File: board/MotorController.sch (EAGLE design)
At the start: 35 parts, among them IC1 ATMEGA328P-PU, Q1 IPP80P03P4L-04, Q2 16Mhz, T1 BT137-600E

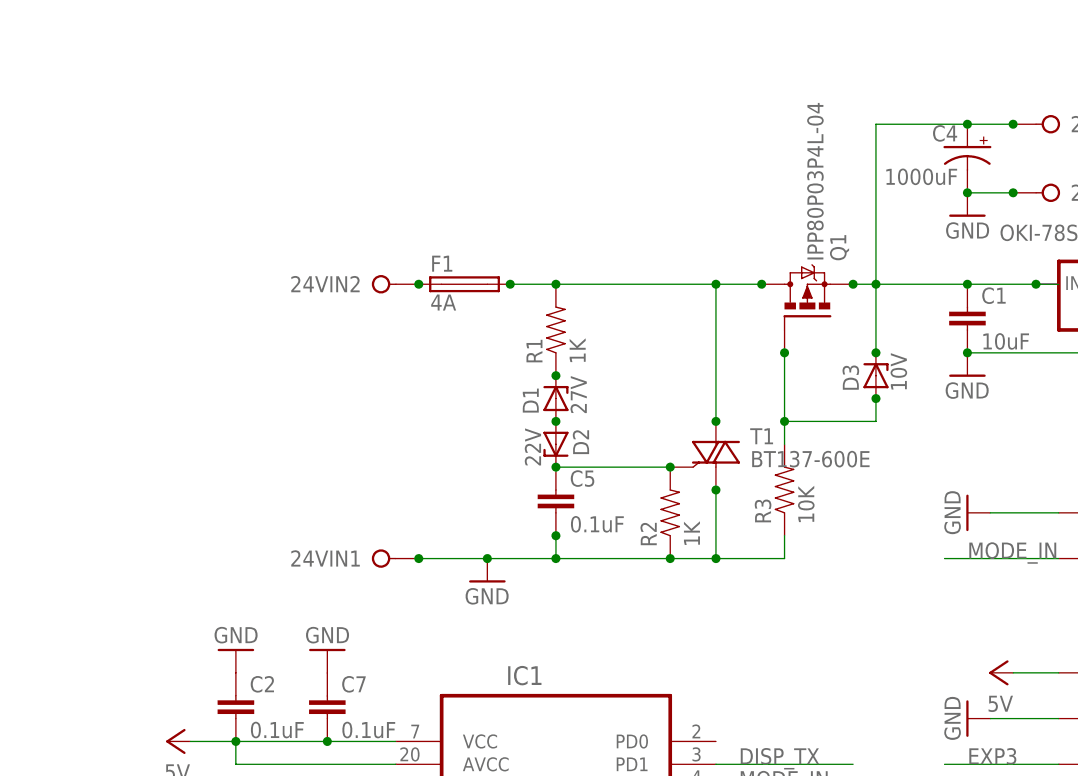
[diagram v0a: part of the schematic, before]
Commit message: Add soft-start capability to avoid high inrush current
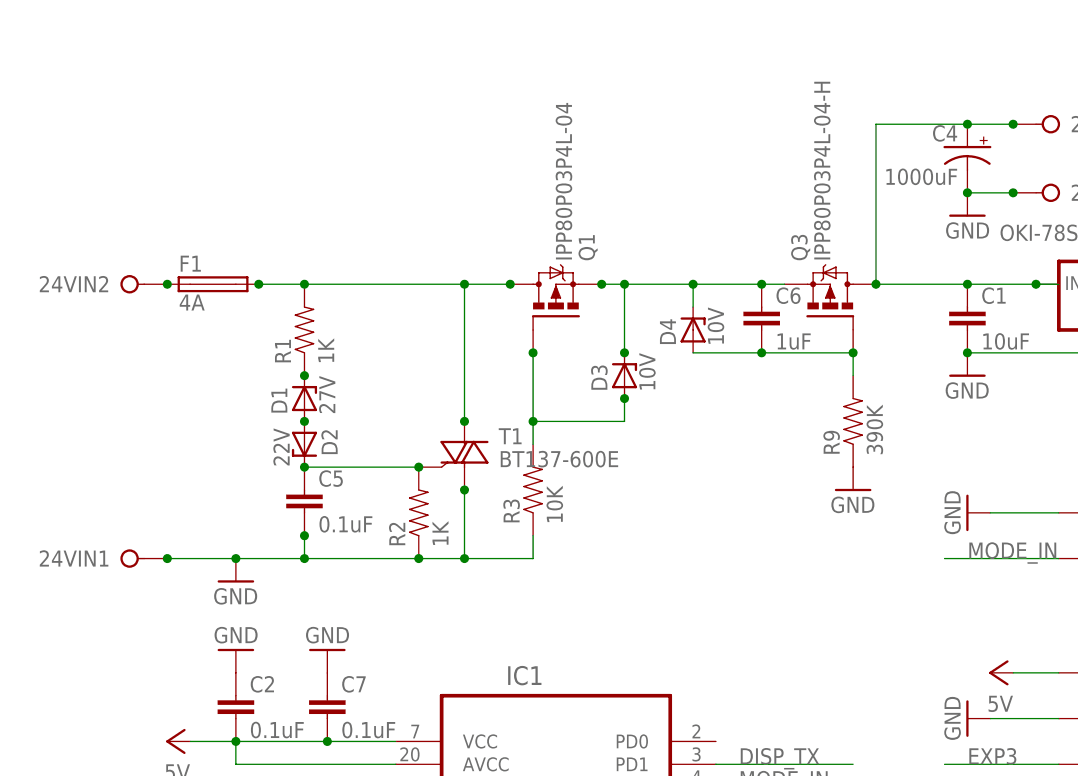
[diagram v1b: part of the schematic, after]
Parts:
- added C6: 1uF, SaintGimp:CAPACITOR-2.5MM
- added D4: 10V, SaintGimp:ZENER-7.5
- added Q3: IPP80P03P4L-04-H, SaintGimp:IPP80P03P4L-04-H
- added R9: 390K, SaintGimp:RESISTOR-7.5MM
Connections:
- new net N$11: C6.2, D4.A, Q3.G, R9.2
- new net N$9: C6.1, D3.C, D4.C, Q1.S, Q3.S
- net 24V-PROTECTED: now also Q3.D; no longer D3.C, Q1.S
- net GND: now also R9.1
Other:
- moved on the sheet: 24VIN1, 24VIN2, C5, D1, D2, D3, F1, Q1, R1, R2, R3, T1

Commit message: Many changes for version 3
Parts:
- removed C12: 20pF, SaintGimp:CAPACITOR-2.5MM
- removed Q3: IPP80P03P4L-04-H, SaintGimp:IPP80P03P4L-04-H
- added C10: 1uF, SaintGimp:CAPACITOR-2.5MM
- added Y1: 16Mhz, SaintGimp:CRYSTAL-V
- C1: value 10uF -> 0.1uF; device SaintGimp:CAPACITOR-5MM -> SaintGimp:CAPACITOR-2.5MM
- C11: value 20pF -> 1000uF; device SaintGimp:CAPACITOR-2.5MM -> SaintGimp:CAP-POL-25-14
- C3: value 10uF -> 20pF; device SaintGimp:CAPACITOR-5MM -> SaintGimp:CAPACITOR-2.5MM
- C4: value 1000uF -> 1uF; device SaintGimp:CAP-POL-25-14 -> SaintGimp:CAPACITOR-2.5MM
- C5: value 0.1uF -> 1uF
- C6: value 1uF -> 20pF
- C8, C9: value 1uF -> 10uF; device SaintGimp:CAPACITOR-2.5MM -> SaintGimp:CAPACITOR-5MM
- D1: value 27V -> 22V
- D2: value 22V -> 27V
- Q2: value 16Mhz -> SUP75P03-07-H; device SaintGimp:CRYSTAL-V -> SaintGimp:SUP75P03-07-H
- R1: value 1K -> 68
- R2: value 1K -> 10K
- R3: value 10K -> 220
- R5: value 220 -> 1K
- R6: value 68 -> 1K
- R7: value 390K -> 576K
- renumbered R9 to R7
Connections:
- net 24V: now also R6.2; no longer R1.2
- net 24V-PROTECTED: now also C11.+, C8.1, Q2.D; no longer C1.1, C4.+, Q3.D
- net CRYSTAL1: now also C3.1, Y1.2; no longer C11.1, Q2.2
- net CRYSTAL2: now also C6.1, Y1.1; no longer C12.1, Q2.1
- net DISP_TX: now also R1.2; no longer R6.2
- net GND: now also C1.1, C11.-, C4.2, C6.2, C7.2, R5.1, R8.1; no longer C1.2, C11.2, C12.2, C4.-, C7.1, R2.1, R3.1
- net N$1: now also C4.1, R3.1; no longer C8.1, R5.1
- net N$10: now also C5.1, R4.2; no longer C9.1, R5.2
- net N$11: now also C10.2, Q2.G; no longer C6.2, Q3.G
- net N$4: now also R8.2; no longer R3.2
- net N$5: now also D2.C, R6.1; no longer D1.C, R1.1
- net N$7: now also C7.1, D1.C, R5.2; no longer C5.1, D2.C, R2.2
- net N$8: now also R1.1; no longer R6.1
- net N$9: now also C10.1, Q2.S; no longer C6.1, Q3.S
- net RESET: now also R2.2; no longer R8.2
- net SPD_OUT: now also R3.2; no longer R4.2
- net VCC: now also C1.2, C9.1, R2.1; no longer C3.1, C7.2, R8.1
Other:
- moved on the sheet: C1, C3, C5, C6, C7, C8, C9, D1, D2, R1, R2, R3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

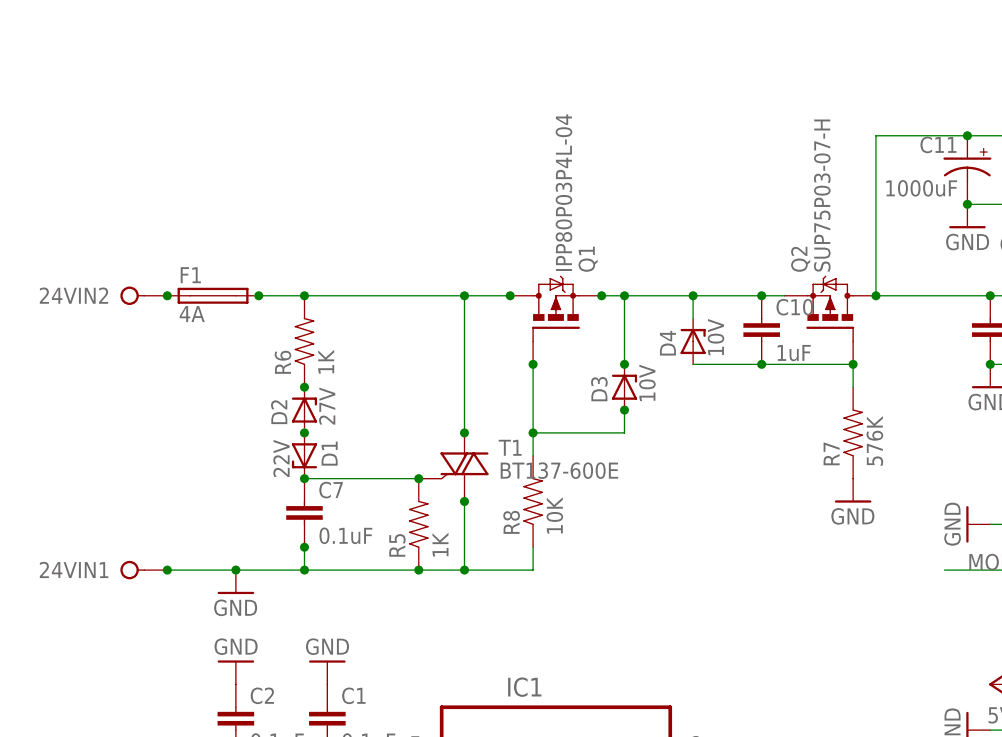
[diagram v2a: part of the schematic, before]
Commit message: Tweak TO220 packages and add board heatsink
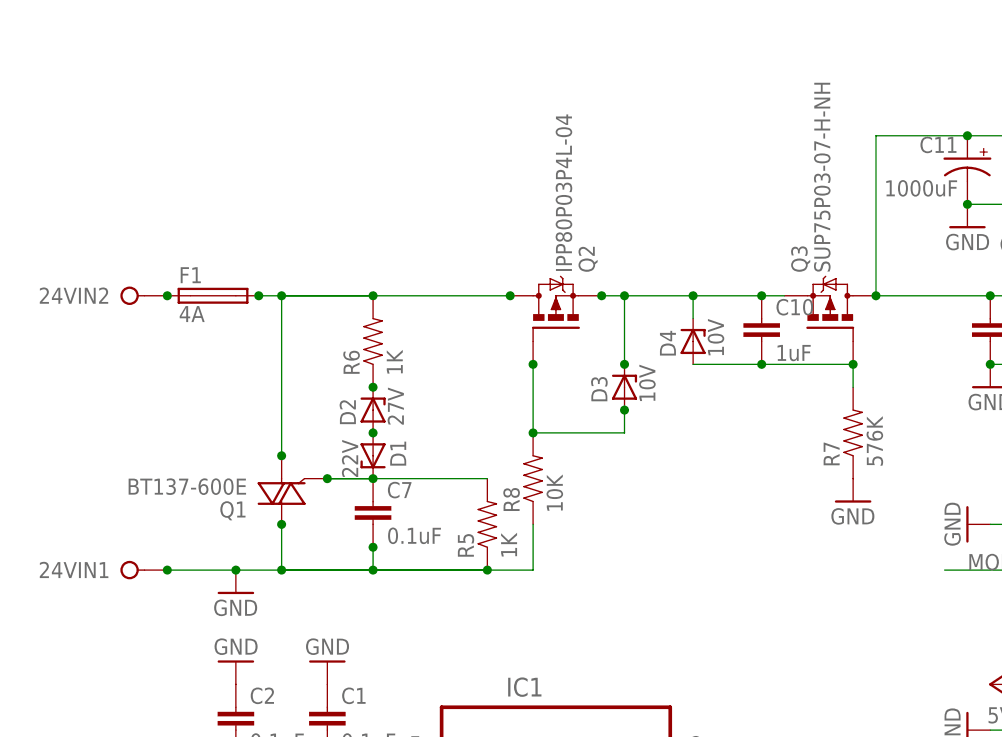
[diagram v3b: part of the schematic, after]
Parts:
- removed T1: BT137-600E, SaintGimp:TRIAC-H
- added Q3: SUP75P03-07-H-NH, SaintGimp:SUP75P03-07-H-NH
- Q1: value IPP80P03P4L-04 -> BT137-600E; device SaintGimp:IPP80P03P4L-04-H -> SaintGimp:TRIAC-H-NH
- Q2: value SUP75P03-07-H -> IPP80P03P4L-04; device SaintGimp:SUP75P03-07-H -> SaintGimp:IPP80P03P4L-04-H-NH
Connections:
- net 24V: now also Q1.A1, Q2.D; no longer Q1.D, T1.A2
- net 24V-PROTECTED: now also Q3.D; no longer Q2.D
- net GND: now also Q1.A2; no longer T1.A1
- net N$11: now also Q3.G; no longer Q2.G
- net N$4: now also Q2.G; no longer Q1.G
- net N$7: now also Q1.G; no longer T1.G
- net N$9: now also Q3.S; no longer Q1.S
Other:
- moved on the sheet: C7, D1, D2, Q2, R5, R6, R8
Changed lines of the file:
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@@
 <part name="C11" library="SaintGimp" deviceset="CAP-POL" device="-25-14" value="1000uF"/>
 <part name="F1" library="SaintGimp" deviceset="FUSE" device="" value="4A"/>
-<part name="T1" library="SaintGimp" deviceset="TRIAC" device="-H" value="BT137-600E"/>
+<part name="Q1" library="SaintGimp" deviceset="TRIAC" device="-H-NH" value="BT137-600E"/>
 <part name="D1" library="SaintGimp" deviceset="ZENER" device="-7.5" value="22V"/>
 <part name="D2" library="SaintGimp" deviceset="ZENER" device="-7.5" value="27V"/>
@@
 <part name="C7" library="SaintGimp" deviceset="CAPACITOR-*" device="2.5MM" value="0.1uF"/>
 <part name="R5" library="SaintGimp" deviceset="RESISTOR-*" device="7.5MM" value="1K"/>
-<part name="Q1" library="SaintGimp" deviceset="IPP80P03P4L-04" device="-H" value="IPP80P03P4L-04"/>
+<part name="Q2" library="SaintGimp" deviceset="IPP80P03P4L-04" device="-H-NH" value="IPP80P03P4L-04"/>
 <part name="R8" library="SaintGimp" deviceset="RESISTOR-*" device="7.5MM" value="10K"/>
 <part name="D3" library="SaintGimp" deviceset="ZENER" device="-7.5" value="10V"/>
@@
 <part name="5V7" library="SaintGimp" deviceset="VCC" device="" value="5V"/>
 <part name="GND18" library="SaintGimp" deviceset="GND" device=""/>
-<part name="Q2" library="SaintGimp" deviceset="SUP75P03-07" device="-H"/>
+<part name="Q3" library="SaintGimp" deviceset="SUP75P03-07" device="-H-NH" value="SUP75P03-07-H-NH"/>
 <part name="R7" library="SaintGimp" deviceset="RESISTOR-*" device="7.5MM" value="576K"/>
 <part name="GND19" library="SaintGimp" deviceset="GND" device=""/>
@@
 <instance part="C11" gate="G$1" x="40.64" y="68.58" rot="MR0"/>
 <instance part="F1" gate="G$1" x="-43.18" y="53.34"/>
-<instance part="T1" gate="G$1" x="-15.24" y="33.02"/>
-<instance part="D1" gate="G$1" x="-33.02" y="35.56" rot="R270"/>
-<instance part="D2" gate="G$1" x="-33.02" y="40.64" rot="R90"/>
-<instance part="R6" gate="G$1" x="-33.02" y="48.26" rot="R90"/>
-<instance part="C7" gate="G$1" x="-33.02" y="27.94"/>
-<instance part="R5" gate="G$1" x="-20.32" y="27.94" rot="R90"/>
-<instance part="Q1" gate="G$1" x="-5.08" y="50.8" rot="MR90"/>
-<instance part="R8" gate="G$1" x="-7.62" y="30.48" rot="R90"/>
+<instance part="Q1" gate="G$1" x="-35.56" y="33.02" rot="R180"/>
+<instance part="D1" gate="G$1" x="-25.4" y="35.56" rot="R270"/>
+<instance part="D2" gate="G$1" x="-25.4" y="40.64" rot="R90"/>
+<instance part="R6" gate="G$1" x="-25.4" y="48.26" rot="R90"/>
+<instance part="C7" gate="G$1" x="-25.4" y="27.94"/>
+<instance part="R5" gate="G$1" x="-12.7" y="27.94" rot="R90"/>
+<instance part="Q2" gate="G$1" x="-5.08" y="50.8" rot="MR90"/>
+<instance part="R8" gate="G$1" x="-7.62" y="33.02" rot="R90"/>
 <instance part="D3" gate="G$1" x="2.54" y="43.18" rot="R90"/>
 <instance part="C9" gate="G$1" x="68.58" y="48.26"/>
@@
 <instance part="FRONT" gate="4" x="55.88" y="-5.08" rot="R180"/>
 <instance part="FRONT" gate="3" x="55.88" y="0" rot="R180"/>
-<instance part="Q2" gate="G$1" x="25.4" y="50.8" rot="R90"/>
+<instance part="Q3" gate="G$1" x="25.4" y="50.8" rot="R90"/>
 <instance part="R7" gate="G$1" x="27.94" y="38.1" rot="R90"/>
 <instance part="GND19" gate="1" x="27.94" y="30.48"/>
@@
 </segment>
 <segment>
-<pinref part="T1" gate="G$1" pin="A1"/>
-<wire x1="-15.24" y1="30.48" x2="-15.24" y2="22.86" width="0.1524" layer="91"/>
+<pinref part="Q1" gate="G$1" pin="A2"/>
+<wire x1="-35.56" y1="27.94" x2="-35.56" y2="22.86" width="0.1524" layer="91"/>
 <pinref part="R5" gate="G$1" pin="1"/>
-<wire x1="-15.24" y1="22.86" x2="-20.32" y2="22.86" width="0.1524" layer="91"/>
-<wire x1="-20.32" y1="22.86" x2="-33.02" y2="22.86" width="0.1524" layer="91"/>
-<junction x="-20.32" y="22.86"/>
+<wire x1="-35.56" y1="22.86" x2="-12.7" y2="22.86" width="0.1524" layer="91"/>
+<wire x1="-12.7" y1="22.86" x2="-25.4" y2="22.86" width="0.1524" layer="91"/>
+<junction x="-12.7" y="22.86"/>
 <pinref part="C7" gate="G$1" pin="2"/>
-<wire x1="-33.02" y1="22.86" x2="-40.64" y2="22.86" width="0.1524" layer="91"/>
+<wire x1="-25.4" y1="22.86" x2="-35.56" y2="22.86" width="0.1524" layer="91"/>
+<wire x1="-35.56" y1="22.86" x2="-40.64" y2="22.86" width="0.1524" layer="91"/>
 <wire x1="-40.64" y1="22.86" x2="-48.26" y2="22.86" width="0.1524" layer="91"/>
-<wire x1="-33.02" y1="25.4" x2="-33.02" y2="22.86" width="0.1524" layer="91"/>
-<junction x="-33.02" y="22.86"/>
+<wire x1="-25.4" y1="25.4" x2="-25.4" y2="22.86" width="0.1524" layer="91"/>
+<junction x="-25.4" y="22.86"/>
 <pinref part="R8" gate="G$1" pin="1"/>
-<wire x1="-7.62" y1="25.4" x2="-7.62" y2="22.86" width="0.1524" layer="91"/>
-<wire x1="-7.62" y1="22.86" x2="-15.24" y2="22.86" width="0.1524" layer="91"/>
-<junction x="-15.24" y="22.86"/>
+<wire x1="-7.62" y1="27.94" x2="-7.62" y2="22.86" width="0.1524" layer="91"/>
+<wire x1="-7.62" y1="22.86" x2="-35.56" y2="22.86" width="0.1524" layer="91"/>
+<junction x="-35.56" y="22.86"/>
 <pinref part="24VIN" gate="1" pin="KL"/>
-<junction x="-15.24" y="30.48"/>
+<junction x="-35.56" y="27.94"/>
 <pinref part="GND4" gate="1" pin="GND"/>
 <junction x="-40.64" y="22.86"/>
 <junction x="-48.26" y="22.86"/>
-<junction x="-33.02" y="25.4"/>
+<junction x="-25.4" y="25.4"/>
 </segment>
 <segment>
@@
 <pinref part="R6" gate="G$1" pin="1"/>
 <pinref part="D2" gate="G$1" pin="C"/>
-<junction x="-33.02" y="43.18"/>
+<junction x="-25.4" y="43.18"/>
 </segment>
 </net>
@@
 <pinref part="D2" gate="G$1" pin="A"/>
 <pinref part="D1" gate="G$1" pin="A"/>
-<junction x="-33.02" y="38.1"/>
+<junction x="-25.4" y="38.1"/>
 </segment>
 </net>
 <net name="N$7" class="0">
 <segment>
-<pinref part="T1" gate="G$1" pin="G"/>
+<pinref part="Q1" gate="G$1" pin="G"/>
 <pinref part="D1" gate="G$1" pin="C"/>
-<wire x1="-20.32" y1="33.02" x2="-33.02" y2="33.02" width="0.1524" layer="91"/>
+<wire x1="-30.48" y1="33.02" x2="-25.4" y2="33.02" width="0.1524" layer="91"/>
 <pinref part="C7" gate="G$1" pin="1"/>
-<junction x="-33.02" y="33.02"/>
+<junction x="-25.4" y="33.02"/>
 <pinref part="R5" gate="G$1" pin="2"/>
-<junction x="-20.32" y="33.02"/>
+<junction x="-30.48" y="33.02"/>
+<wire x1="-30.48" y1="33.02" x2="-12.7" y2="33.02" width="0.1524" layer="91"/>
 </segment>
 </net>
@@
 <pinref part="F1" gate="G$1" pin="2"/>
 <pinref part="R6" gate="G$1" pin="2"/>
-<wire x1="-33.02" y1="53.34" x2="-38.1" y2="53.34" width="0.1524" layer="91"/>
-<junction x="-33.02" y="53.34"/>
-<wire x1="-33.02" y1="53.34" x2="-15.24" y2="53.34" width="0.1524" layer="91"/>
-<pinref part="T1" gate="G$1" pin="A2"/>
-<wire x1="-15.24" y1="38.1" x2="-15.24" y2="53.34" width="0.1524" layer="91"/>
-<pinref part="Q1" gate="G$1" pin="D"/>
-<wire x1="-10.16" y1="53.34" x2="-15.24" y2="53.34" width="0.1524" layer="91"/>
-<junction x="-15.24" y="53.34"/>
+<junction x="-25.4" y="53.34"/>
+<wire x1="-35.56" y1="53.34" x2="-38.1" y2="53.34" width="0.1524" layer="91"/>
+<wire x1="-25.4" y1="53.34" x2="-35.56" y2="53.34" width="0.1524" layer="91"/>
+<pinref part="Q1" gate="G$1" pin="A1"/>
+<wire x1="-35.56" y1="35.56" x2="-35.56" y2="53.34" width="0.1524" layer="91"/>
+<pinref part="Q2" gate="G$1" pin="D"/>
+<wire x1="-10.16" y1="53.34" x2="-35.56" y2="53.34" width="0.1524" layer="91"/>
+<junction x="-35.56" y="53.34"/>
 <junction x="-10.16" y="53.34"/>
-<junction x="-15.24" y="38.1"/>
+<junction x="-35.56" y="35.56"/>
 <junction x="-38.1" y="53.34"/>
 </segment>
@@
 <net name="N$4" class="0">
 <segment>
-<pinref part="Q1" gate="G$1" pin="G"/>
+<pinref part="Q2" gate="G$1" pin="G"/>
 <pinref part="R8" gate="G$1" pin="2"/>
 <wire x1="-7.62" y1="45.72" x2="-7.62" y2="38.1" width="0.1524" layer="91"/>
 <pinref part="D3" gate="G$1" pin="A"/>
-<wire x1="-7.62" y1="38.1" x2="-7.62" y2="35.56" width="0.1524" layer="91"/>
 <wire x1="2.54" y1="40.64" x2="2.54" y2="38.1" width="0.1524" layer="91"/>
 <wire x1="2.54" y1="38.1" x2="-7.62" y2="38.1" width="0.1524" layer="91"/>
@@
 <pinref part="C8" gate="G$1" pin="1"/>
 <junction x="43.18" y="53.34"/>
-<pinref part="Q2" gate="G$1" pin="D"/>
+<pinref part="Q3" gate="G$1" pin="D"/>
 <junction x="30.48" y="53.34"/>
 <pinref part="C11" gate="G$1" pin="+"/>
@@
 <net name="N$9" class="1">
 <segment>
-<pinref part="Q1" gate="G$1" pin="S"/>
+<pinref part="Q2" gate="G$1" pin="S"/>
 <junction x="0" y="53.34"/>
-<pinref part="Q2" gate="G$1" pin="S"/>
+<pinref part="Q3" gate="G$1" pin="S"/>
 <wire x1="2.54" y1="53.34" x2="10.16" y2="53.34" width="0.1524" layer="91"/>
 <wire x1="10.16" y1="53.34" x2="17.78" y2="53.34" width="0.1524" layer="91"/>
@@
 <segment>
 <pinref part="R7" gate="G$1" pin="2"/>
-<pinref part="Q2" gate="G$1" pin="G"/>
+<pinref part="Q3" gate="G$1" pin="G"/>
 <wire x1="27.94" y1="43.18" x2="27.94" y2="45.72" width="0.1524" layer="91"/>
 <pinref part="C10" gate="G$1" pin="2"/>
